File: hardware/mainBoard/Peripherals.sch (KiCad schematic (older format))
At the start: 4 parts

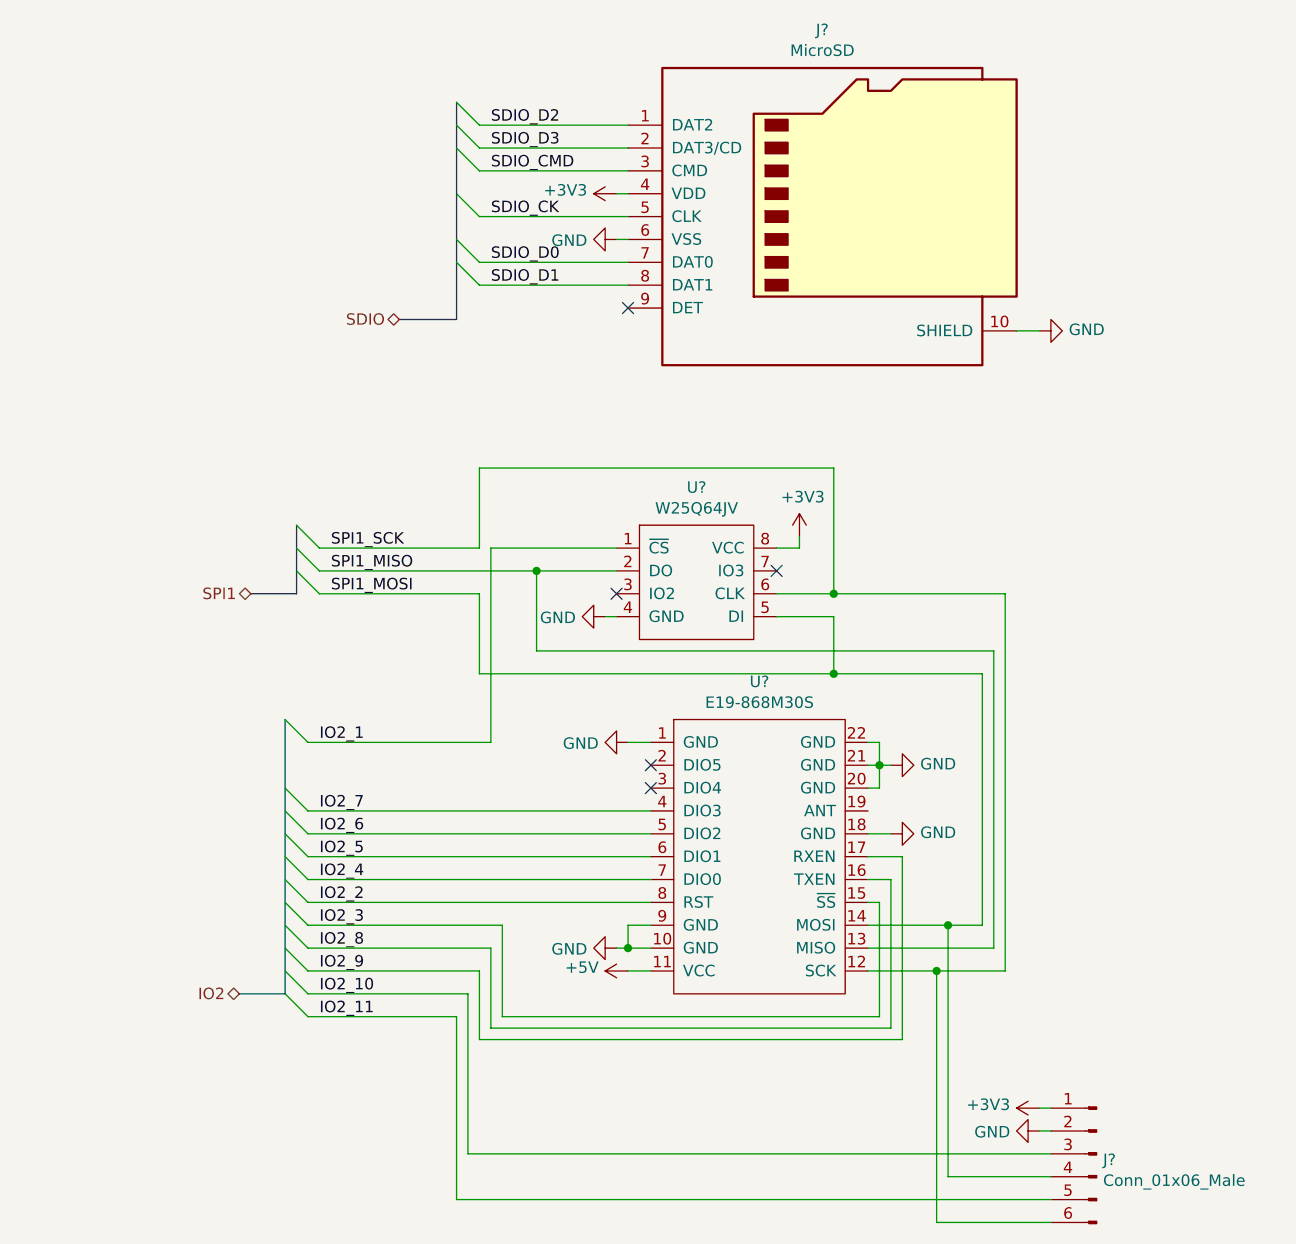
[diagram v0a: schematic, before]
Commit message: Ended schematic, created some pcb footprints
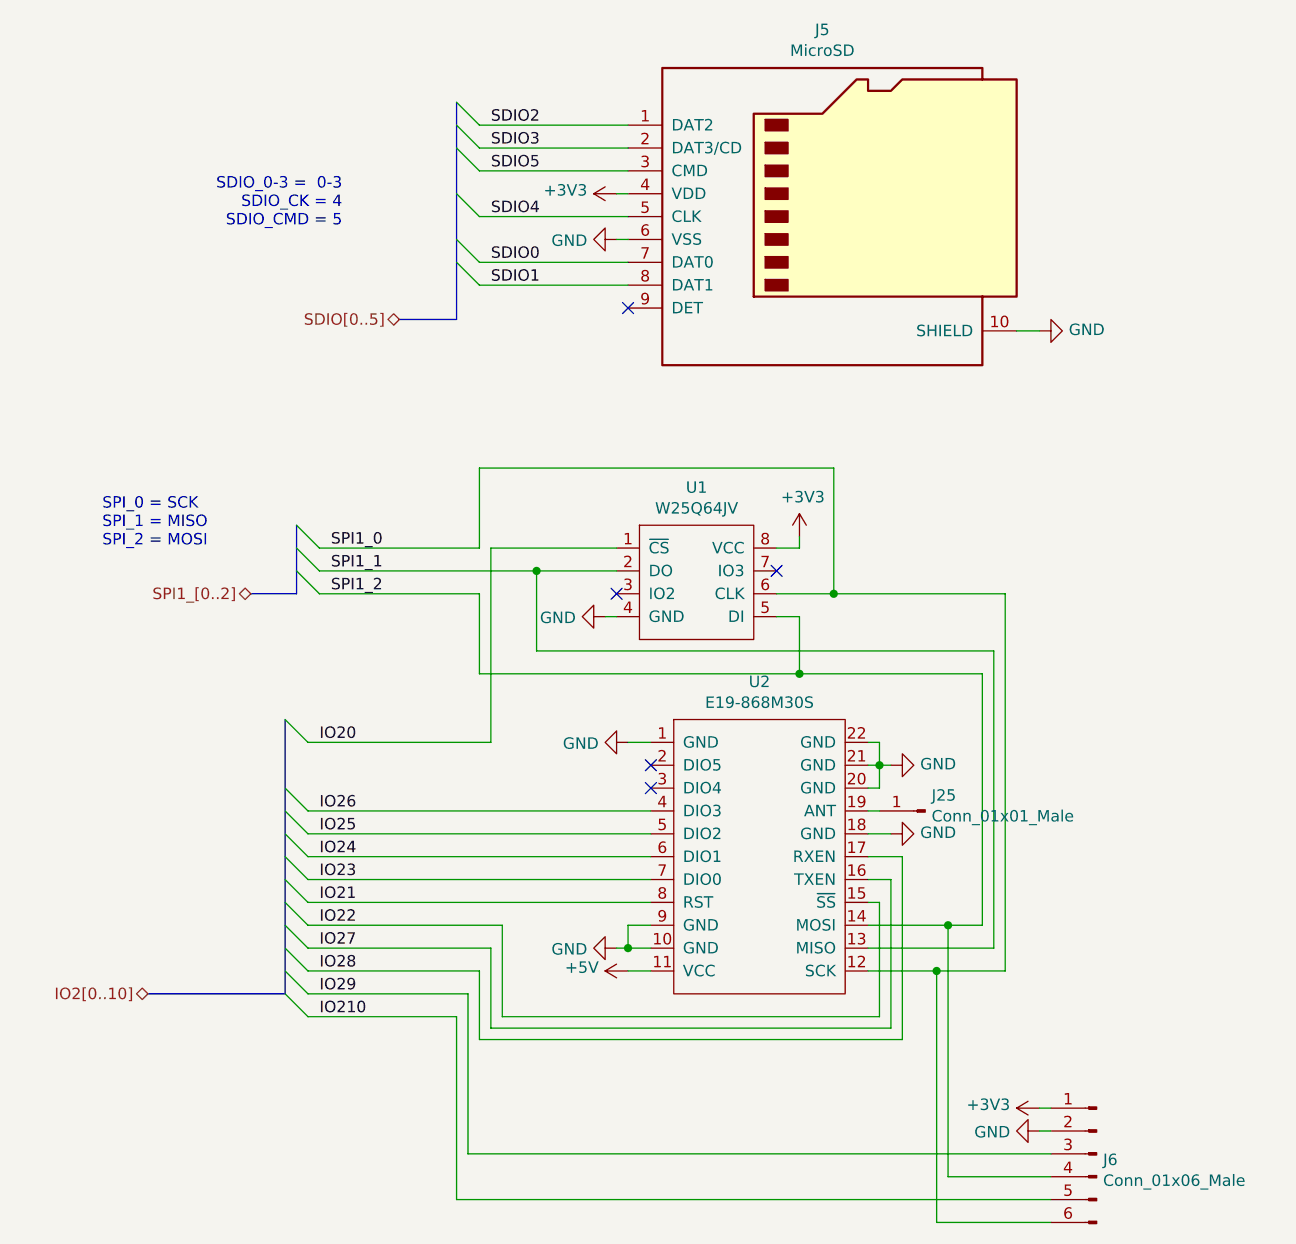
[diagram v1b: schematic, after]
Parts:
- removed U?: W25Q64JV, symbol Chinaland:W25Q64JV
- added J25: Conn_01x01_Male, Connector_Wire:SolderWirePad_1x01_SMD_5x10mm, symbol Connector:Conn_01x01_Male
- added U1: W25Q64JV, Package_SO:SOIC-8_5.23x5.23mm_P1.27mm, symbol Chinaland:W25Q64JV
- J5: renamed from J?; footprint (none) -> chinalandfoot:MicroSD-KoreanHroparts
- J6: renamed from J?; footprint (none) -> Connector_JST:JST_XH_B6B-XH-A_1x06_P2.50mm_Vertical
- U2: renamed from U?; footprint (none) -> chinalandfoot:E19-868MS1W
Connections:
- net +3V3: now also U1.8 (VCC)
- net GND: now also U1.4 (GND)
- net at U2.19 (ANT): now also J25.1 (Pin_1)
- net IO2_10 renamed IO29
- net IO2_11 renamed IO210
- net IO2_2 renamed IO21
- net IO2_3 renamed IO22
- net IO2_4 renamed IO23
- net IO2_5 renamed IO24
- net IO2_6 renamed IO25
- net IO2_7 renamed IO26
- net IO2_8 renamed IO27
- net IO2_9 renamed IO28
- net SDIO_CK renamed SDIO4
- net SDIO_CMD renamed SDIO5
- net SDIO_D0 renamed SDIO0
- net SDIO_D1 renamed SDIO1
- net SDIO_D2 renamed SDIO2
- net SDIO_D3 renamed SDIO3
- net SPI1_MISO renamed SPI1_1
- net SPI1_1: now also U1.2 (DO)
- net SPI1_MOSI renamed SPI1_2
- net SPI1_2: now also U1.5 (DI)
- net SPI1_SCK renamed SPI1_0
- net SPI1_0: now also U1.6 (CLK)
- new net IO20: U1.1 (~CS)
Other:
- note added: "SDIO_0-3 = 0-3\nSDIO_CK = 4\nSDIO_CMD = 5"
- note added: "SPI_0 = SCK\nSPI_1 = MISO\nSPI_2 = MOSI"
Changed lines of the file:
@@
 $Descr A4 11693 8268
 encoding utf-8
-Sheet 3 8
+Sheet 3 10
 Title ""
 Date ""
@@
 $EndDescr
 $Comp
-L Chinaland:MicroSD J?
+L Chinaland:MicroSD J5
 U 1 1 5DEE176A
 P 4550 2650
-F 0 "J?" H 4550 3367 50  0000 C CNN
+F 0 "J5" H 4550 3367 50  0000 C CNN
 F 1 "MicroSD" H 4550 3276 50  0000 C CNN
-F 2 "" H 4550 2650 50  0001 C CNN
+F 2 "chinalandfoot:MicroSD-KoreanHroparts" H 4550 2650 50  0001 C CNN
 F 3 "" H 4550 2650 50  0001 C CNN
 	1    4550 2650
@@
 $EndComp
 $Comp
-L Chinaland:E19-868M30S U?
+L Chinaland:E19-868M30S U2
 U 1 1 5DEE3C98
 P 4250 5500
-F 0 "U?" H 4275 6215 50  0000 C CNN
+F 0 "U2" H 4275 6215 50  0000 C CNN
 F 1 "E19-868M30S" H 4275 6124 50  0000 C CNN
-F 2 "" H 4250 5450 50  0001 C CNN
+F 2 "chinalandfoot:E19-868MS1W" H 4250 5450 50  0001 C CNN
 F 3 "" H 4250 5450 50  0001 C CNN
 	1    4250 5500
 	1    0    0    -1
 $EndComp
-$Comp
-L Chinaland:W25Q64JV U?
-U 1 1 5DEE972F
-P 4000 4350
-F 0 "U?" H 4000 4765 50  0000 C CNN
-F 1 "W25Q64JV" H 4000 4674 50  0000 C CNN
-F 2 "" H 4000 4350 50  0001 C CNN
-F 3 "" H 4000 4350 50  0001 C CNN
-	1    4000 4350
-	1    0    0    -1
-$EndComp
 Text HLabel 2050 4400 0    50   BiDi ~ 0
-SPI1
-Text HLabel 2000 6150 0    50   BiDi ~ 0
-IO2
+SPI1_[0..2]
+Text HLabel 1600 6150 0    50   BiDi ~ 0
+IO2[0..10]
 Wire Bus Line
 	2050 4400 2250 4400
@@
 Wire Wire Line
 	4600 3850 4600 4400
-Wire Wire Line
-	4600 4400 4350 4400
-Wire Wire Line
-	4350 4500 4600 4500
-Wire Wire Line
-	4600 4500 4600 4750
-Wire Wire Line
-	3050 4750 4600 4750
 Text Label 2400 4200 0    50   ~ 0
-SPI1_SCK
+SPI1_0
 Text Label 2400 4300 0    50   ~ 0
-SPI1_MISO
+SPI1_1
 Text Label 2400 4400 0    50   ~ 0
-SPI1_MOSI
-$Comp
-L power:GND #PWR?
+SPI1_2
+$Comp
+L power:GND #PWR07
 U 1 1 5DF073AA
 P 3600 4500
-F 0 "#PWR?" H 3600 4250 50  0001 C CNN
+F 0 "#PWR07" H 3600 4250 50  0001 C CNN
 F 1 "GND" V 3605 4372 50  0000 R CNN
 F 2 "" H 3600 4500 50  0001 C CNN
@@
 	3600 4500 3650 4500
 Wire Bus Line
-	2000 6150 2200 6150
+	1600 6150 2200 6150
 Entry Wire Line
 	2200 4950 2300 5050
@@
 Wire Wire Line
 	3100 5050 2300 5050
-Text Label 2350 5050 0    50   ~ 0
-IO2_1
-$Comp
-L power:+3V3 #PWR?
+$Comp
+L power:+3V3 #PWR013
 U 1 1 5DF0A362
 P 4450 4150
-F 0 "#PWR?" H 4450 4000 50  0001 C CNN
+F 0 "#PWR013" H 4450 4000 50  0001 C CNN
 F 1 "+3V3" H 4465 4323 50  0000 C CNN
 F 2 "" H 4450 4150 50  0001 C CNN
@@
 	3100 4200 3100 5050
 $Comp
-L power:GND #PWR?
+L power:GND #PWR014
 U 1 1 5DF6D39B
 P 4850 5150
-F 0 "#PWR?" H 4850 4900 50  0001 C CNN
+F 0 "#PWR014" H 4850 4900 50  0001 C CNN
 F 1 "GND" V 4855 5022 50  0000 R CNN
 F 2 "" H 4850 5150 50  0001 C CNN
@@
 	4800 5250 4800 5150
 $Comp
-L power:GND #PWR?
+L power:GND #PWR011
 U 1 1 5DF6FC7C
 P 3700 5050
-F 0 "#PWR?" H 3700 4800 50  0001 C CNN
+F 0 "#PWR011" H 3700 4800 50  0001 C CNN
 F 1 "GND" V 3705 4922 50  0000 R CNN
 F 2 "" H 3700 5050 50  0001 C CNN
@@
 	3700 5050 3800 5050
 $Comp
-L power:GND #PWR?
+L power:GND #PWR015
 U 1 1 5DF70374
 P 4850 5450
-F 0 "#PWR?" H 4850 5200 50  0001 C CNN
+F 0 "#PWR015" H 4850 5200 50  0001 C CNN
 F 1 "GND" V 4855 5322 50  0000 R CNN
 F 2 "" H 4850 5450 50  0001 C CNN
@@
 	4850 5450 4750 5450
 $Comp
-L power:GND #PWR?
+L power:GND #PWR010
 U 1 1 5DF70E78
 P 3650 5950
-F 0 "#PWR?" H 3650 5700 50  0001 C CNN
+F 0 "#PWR010" H 3650 5700 50  0001 C CNN
 F 1 "GND" V 3655 5822 50  0000 R CNN
 F 2 "" H 3650 5950 50  0001 C CNN
@@
 	2200 5650 2300 5750
 Text Label 2350 5750 0    50   ~ 0
-IO2_2
+IO21
 Text Label 2350 5650 0    50   ~ 0
-IO2_4
+IO23
 Text Label 2350 5550 0    50   ~ 0
-IO2_5
+IO24
 Text Label 2350 5450 0    50   ~ 0
-IO2_6
+IO25
 Text Label 2350 5350 0    50   ~ 0
-IO2_7
-$Comp
-L power:+5V #PWR?
+IO26
+$Comp
+L power:+5V #PWR012
 U 1 1 5DF79F10
 P 3700 6050
-F 0 "#PWR?" H 3700 5900 50  0001 C CNN
+F 0 "#PWR012" H 3700 5900 50  0001 C CNN
 F 1 "+5V" V 3715 6178 50  0000 L CNN
 F 2 "" H 3700 6050 50  0001 C CNN
@@
 Wire Wire Line
 	5350 4400 4600 4400
-Connection ~ 4600 4400
 Wire Wire Line
 	4750 5950 5300 5950
@@
 	5250 5850 5250 4750
 Wire Wire Line
-	5250 4750 4600 4750
-Connection ~ 4600 4750
-Wire Wire Line
 	4750 5750 4800 5750
 Wire Wire Line
@@
 	3050 6050 2300 6050
 Text Label 2350 5850 0    50   ~ 0
-IO2_3
+IO22
 Text Label 2350 5950 0    50   ~ 0
-IO2_8
+IO27
 Text Label 2350 6050 0    50   ~ 0
-IO2_9
+IO28
 NoConn ~ 3800 5150
 NoConn ~ 3800 5250
@@
 	2300 5750 3800 5750
 $Comp
-L power:+3V3 #PWR?
+L power:+3V3 #PWR017
 U 1 1 5DFE0D8D
 P 5500 6650
-F 0 "#PWR?" H 5500 6500 50  0001 C CNN
+F 0 "#PWR017" H 5500 6500 50  0001 C CNN
 F 1 "+3V3" V 5515 6778 50  0000 L CNN
 F 2 "" H 5500 6650 50  0001 C CNN
@@
 $EndComp
 $Comp
-L power:GND #PWR?
+L power:GND #PWR018
 U 1 1 5DFE2A70
 P 5500 6750
-F 0 "#PWR?" H 5500 6500 50  0001 C CNN
+F 0 "#PWR018" H 5500 6500 50  0001 C CNN
 F 1 "GND" V 5505 6622 50  0000 R CNN
 F 2 "" H 5500 6750 50  0001 C CNN
@@
 	2200 6150 2300 6250
 $Comp
-L Connector:Conn_01x06_Male J?
+L Connector:Conn_01x06_Male J6
 U 1 1 5E01FA1B
 P 5750 6850
-F 0 "J?" H 5722 6824 50  0000 R CNN
+F 0 "J6" H 5722 6824 50  0000 R CNN
 F 1 "Conn_01x06_Male" H 5722 6733 50  0000 R CNN
-F 2 "" H 5750 6850 50  0001 C CNN
+F 2 "Connector_JST:JST_XH_B6B-XH-A_1x06_P2.50mm_Vertical" H 5750 6850 50  0001 C CNN
 F 3 "~" H 5750 6850 50  0001 C CNN
 	1    5750 6850
@@
 	2300 6250 2950 6250
 Text Label 2350 6150 0    50   ~ 0
-IO2_10
+IO29
 Text Label 2350 6250 0    50   ~ 0
-IO2_11
+IO210
 Wire Wire Line
 	5500 6750 5550 6750
@@
 	5050 6050 5350 6050
 Text HLabel 2700 3200 0    50   BiDi ~ 0
-SDIO
+SDIO[0..5]
 Text Label 3100 2350 0    50   ~ 0
-SDIO_D2
+SDIO2
 Text Label 3100 2450 0    50   ~ 0
-SDIO_D3
+SDIO3
 Text Label 3100 2550 0    50   ~ 0
-SDIO_CMD
+SDIO5
 Text Label 3100 2750 0    50   ~ 0
-SDIO_CK
+SDIO4
 Text Label 3100 2950 0    50   ~ 0
-SDIO_D0
+SDIO0
 Text Label 3100 3050 0    50   ~ 0
-SDIO_D1
+SDIO1
 NoConn ~ 3700 3150
 Wire Wire Line
@@
 	3650 2850 3700 2850
 $Comp
-L power:GND #PWR?
+L power:GND #PWR09
 U 1 1 5E08C40A
 P 3650 2850
-F 0 "#PWR?" H 3650 2600 50  0001 C CNN
+F 0 "#PWR09" H 3650 2600 50  0001 C CNN
 F 1 "GND" V 3655 2722 50  0000 R CNN
 F 2 "" H 3650 2850 50  0001 C CNN
@@
 	3650 2650 3700 2650
 $Comp
-L power:+3V3 #PWR?
+L power:+3V3 #PWR08
 U 1 1 5E0895DC
 P 3650 2650
-F 0 "#PWR?" H 3650 2500 50  0001 C CNN
+F 0 "#PWR08" H 3650 2500 50  0001 C CNN
 F 1 "+3V3" V 3665 2778 50  0000 L CNN
 F 2 "" H 3650 2650 50  0001 C CNN
@@
 $EndComp
 $Comp
-L power:GND #PWR?
+L power:GND #PWR016
 U 1 1 5E0B2235
 P 5500 3250
-F 0 "#PWR?" H 5500 3000 50  0001 C CNN
+F 0 "#PWR016" H 5500 3000 50  0001 C CNN
 F 1 "GND" V 5505 3122 50  0000 R CNN
 F 2 "" H 5500 3250 50  0001 C CNN
@@
 Wire Wire Line
 	5400 3250 5500 3250
+Text Label 2350 5050 0    50   ~ 0
+IO20
+Text Notes 1400 4200 0    50   ~ 0
+SPI_0 = SCK\nSPI_1 = MISO\nSPI_2 = MOSI
+Text Notes 2450 2800 2    50   ~ 0
+SDIO_0-3 =  0-3\nSDIO_CK = 4\nSDIO_CMD = 5
+$Comp
+L Connector:Conn_01x01_Male J25
+U 1 1 5E360DF2
+P 5000 5350
+F 0 "J25" H 4972 5282 50  0000 R CNN
+F 1 "Conn_01x01_Male" H 4972 5373 50  0000 R CNN
+F 2 "Connector_Wire:SolderWirePad_1x01_SMD_5x10mm" H 5000 5350 50  0001 C CNN
+F 3 "~" H 5000 5350 50  0001 C CNN
+	1    5000 5350
+	-1   0    0    1
+$EndComp
+Wire Wire Line
+	4800 5350 4750 5350
+Wire Wire Line
+	4600 4400 4350 4400
+Connection ~ 4600 4400
+Wire Wire Line
+	4350 4500 4450 4500
+Wire Wire Line
+	4450 4750 5250 4750
+Wire Wire Line
+	3050 4750 4450 4750
+Connection ~ 4450 4750
+Wire Wire Line
+	4450 4500 4450 4750
+$Comp
+L Chinaland:W25Q64JV U1
+U 1 1 5E52ADCC
+P 4000 4350
+F 0 "U1" H 4000 4765 50  0000 C CNN
+F 1 "W25Q64JV" H 4000 4674 50  0000 C CNN
+F 2 "Package_SO:SOIC-8_5.23x5.23mm_P1.27mm" H 4000 4350 50  0001 C CNN
+F 3 "" H 4000 4350 50  0001 C CNN
+	1    4000 4350
+	1    0    0    -1
+$EndComp
 Wire Bus Line
 	2250 4100 2250 4400

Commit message: First working software
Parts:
- J5: URL (none) -> https://lcsc.com/product-detail/Connector-Card-Sockets_XUNP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
- U1: URL (none) -> https://lcsc.com/product-detail/FLASH_Winbond-Elec-W25Q64JV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
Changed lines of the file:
@@
 EESchema Schematic File Version 4
+LIBS:prockeckv2-cache
 EELAYER 30 0
 EELAYER END
@@
 F 2 "chinalandfoot:MicroSD-KoreanHroparts" H 4550 2650 50  0001 C CNN
 F 3 "" H 4550 2650 50  0001 C CNN
+F 4 "https://lcsc.com/product-detail/Connector-Card-Sockets_XUNPU-TF-115_C266620.html" H 4550 2650 50  0001 C CNN "URL"
 	1    4550 2650
 	1    0    0    -1
@@
 F 2 "Package_SO:SOIC-8_5.23x5.23mm_P1.27mm" H 4000 4350 50  0001 C CNN
 F 3 "" H 4000 4350 50  0001 C CNN
+F 4 "https://lcsc.com/product-detail/FLASH_Winbond-Elec-W25Q64JVSSIQ_C83140.html" H 4000 4350 50  0001 C CNN "URL"
 	1    4000 4350
 	1    0    0    -1
